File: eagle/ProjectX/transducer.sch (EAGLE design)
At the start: 34 parts

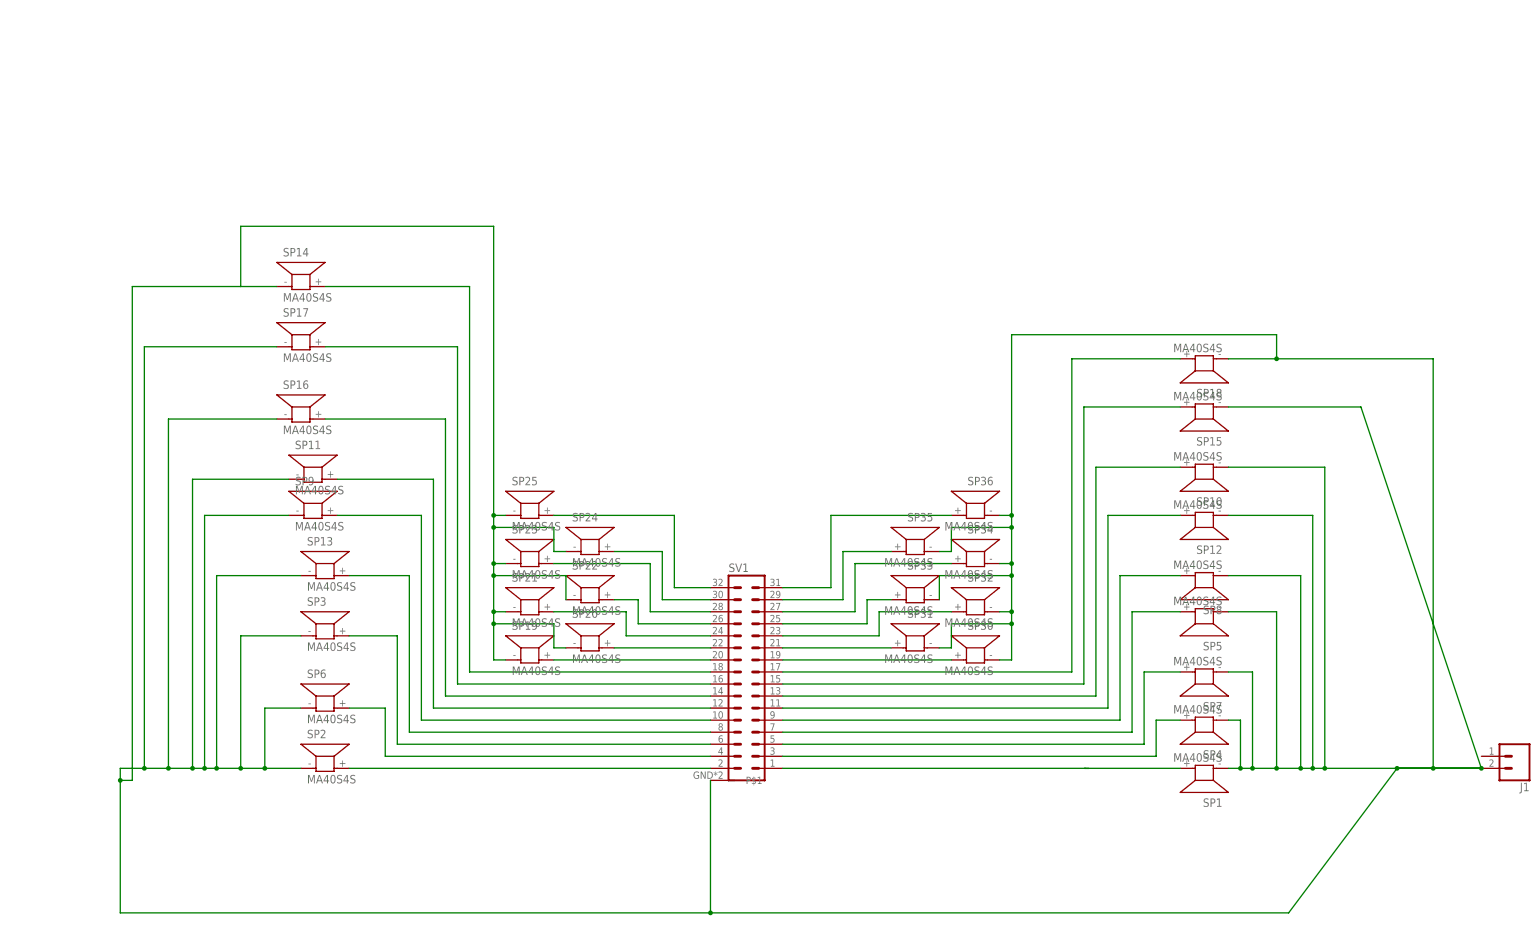
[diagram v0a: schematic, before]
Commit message: Finished the 32 transducer board
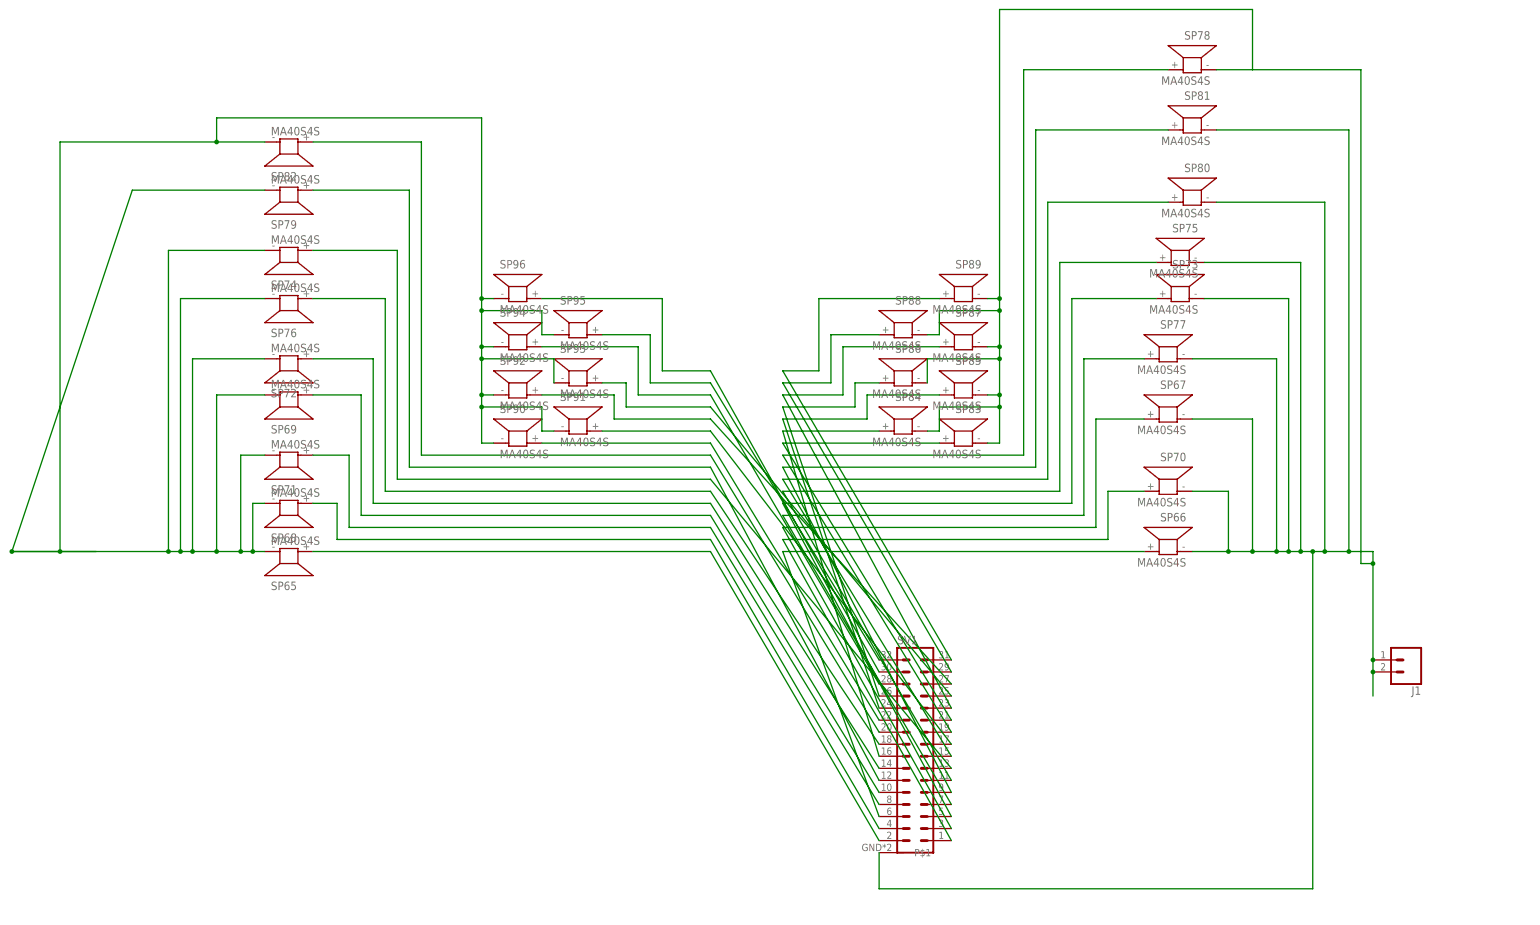
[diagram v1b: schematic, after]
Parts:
- removed SP1, SP10, SP11, SP12, SP13, SP14, SP15, SP16, SP17, SP18, SP19, SP2, SP20, SP21, SP22, SP23, SP24, SP25, SP3, SP30, SP31, SP32, SP33, SP34, SP35, SP36, SP4, SP5, SP6, SP7, SP8, SP9: MA40S4S, transducerlibrary:MA40S4S
- added SP65, SP66, SP67, SP68, SP69, SP70, SP71, SP72, SP73, SP74, SP75, SP76, SP77, SP78, SP79, SP80, SP81, SP82, SP83, SP84, SP85, SP86, SP87, SP88, SP89, SP90, SP91, SP92, SP93, SP94, SP95, SP96: MA40S4S, transducerlibrary:MA40S4S
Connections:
- removed net N$1: SP1.2, SV1.1
- removed net N$10: SP19.2, SV1.20
- removed net N$11: SP8.2, SV1.9
- removed net N$12: SP13.2, SV1.8
- removed net N$13: SP12.2, SV1.11
- removed net N$14: SP9.2, SV1.10
- removed net N$15: SP10.2, SV1.13
- removed net N$16: SP11.2, SV1.12
- removed net N$17: SP16.2, SV1.14
- removed net N$18: SP17.2, SV1.16
- removed net N$19: SP18.2, SV1.17
- removed net N$2: SP15.2, SV1.15
- removed net N$20: SP14.2, SV1.18
- removed net N$22: SP20.2, SV1.22
- removed net N$23: SP21.2, SV1.24
- removed net N$24: SP22.2, SV1.26
- removed net N$25: SP23.2, SV1.28
- removed net N$26: SP24.2, SV1.30
- removed net N$27: SP25.2, SV1.32
- removed net N$28: SP30.2, SV1.19
- removed net N$29: SP31.2, SV1.21
- removed net N$3: SP2.2, SV1.2
- removed net N$30: SP32.2, SV1.23
- removed net N$31: SP33.2, SV1.25
- removed net N$32: SP34.2, SV1.27
- removed net N$33: SP35.2, SV1.29
- removed net N$34: SP36.2, SV1.31
- removed net N$4: SP5.2, SV1.7
- removed net N$5: SP4.2, SV1.3
- removed net N$6: SP6.2, SV1.4
- removed net N$7: SP7.2, SV1.5
- removed net N$9: SP3.2, SV1.6
- new net N$66: SP65.2, SV1.2
- new net N$67: SP66.2, SV1.6
- new net N$68: SP68.2, SV1.4
- new net N$69: SP70.2, SV1.1
- new net N$70: SP67.2, SV1.3
- new net N$71: SP69.2, SV1.10
- new net N$72: SP77.2, SV1.7
- new net N$73: SP76.2, SV1.18
- new net N$74: SP71.2, SV1.8
- new net N$75: SP73.2, SV1.5
- new net N$76: SP74.2, SV1.13
- new net N$77: SP75.2, SV1.11
- new net N$78: SP72.2, SV1.14
- new net N$79: SP80.2, SV1.15
- new net N$80: SP79.2, SV1.12
- new net N$81: SP81.2, SV1.9
- new net N$82: SP82.2, SV1.20
- new net N$83: SP78.2, SV1.19
- new net N$84: SP83.2, SV1.21
- new net N$85: SP84.2, SV1.16
- new net N$86: SP85.2, SV1.24
- new net N$87: SP86.2, SV1.26
- new net N$88: SP87.2, SV1.23
- new net N$89: SP88.2, SV1.29
- new net N$90: SP89.2, SV1.31
- new net N$91: SP90.2, SV1.22
- new net N$92: SP91.2, SV1.17
- new net N$93: SP92.2, SV1.27
- new net N$94: SP93.2, SV1.25
- new net N$95: SP94.2, SV1.28
- new net N$96: SP95.2, SV1.32
- new net N$97: SP96.2, SV1.30
- net GND: now also J1.1, SP65.1, SP66.1, SP67.1, SP68.1, SP69.1, SP70.1, SP71.1, SP72.1, SP73.1, SP74.1, SP75.1, SP76.1, SP77.1, SP78.1, SP79.1, SP80.1, SP81.1, SP82.1, SP83.1, SP84.1, SP85.1, SP86.1, SP87.1, SP88.1, SP89.1, SP90.1, SP91.1, SP92.1, SP93.1, SP94.1, SP95.1, SP96.1; no longer SP1.1, SP10.1, SP11.1, SP12.1, SP13.1, SP14.1, SP15.1, SP16.1, SP17.1, SP18.1, SP19.1, SP2.1, SP20.1, SP21.1, SP22.1, SP23.1, SP24.1, SP25.1, SP3.1, SP30.1, SP31.1, SP32.1, SP33.1, SP34.1, SP35.1, SP36.1, SP4.1, SP5.1, SP6.1, SP7.1, SP8.1, SP9.1
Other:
- moved on the sheet: J1, SV1
